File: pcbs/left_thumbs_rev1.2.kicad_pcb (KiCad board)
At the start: 2 copper layers, 93.5 x 38.7 mm, 12 parts

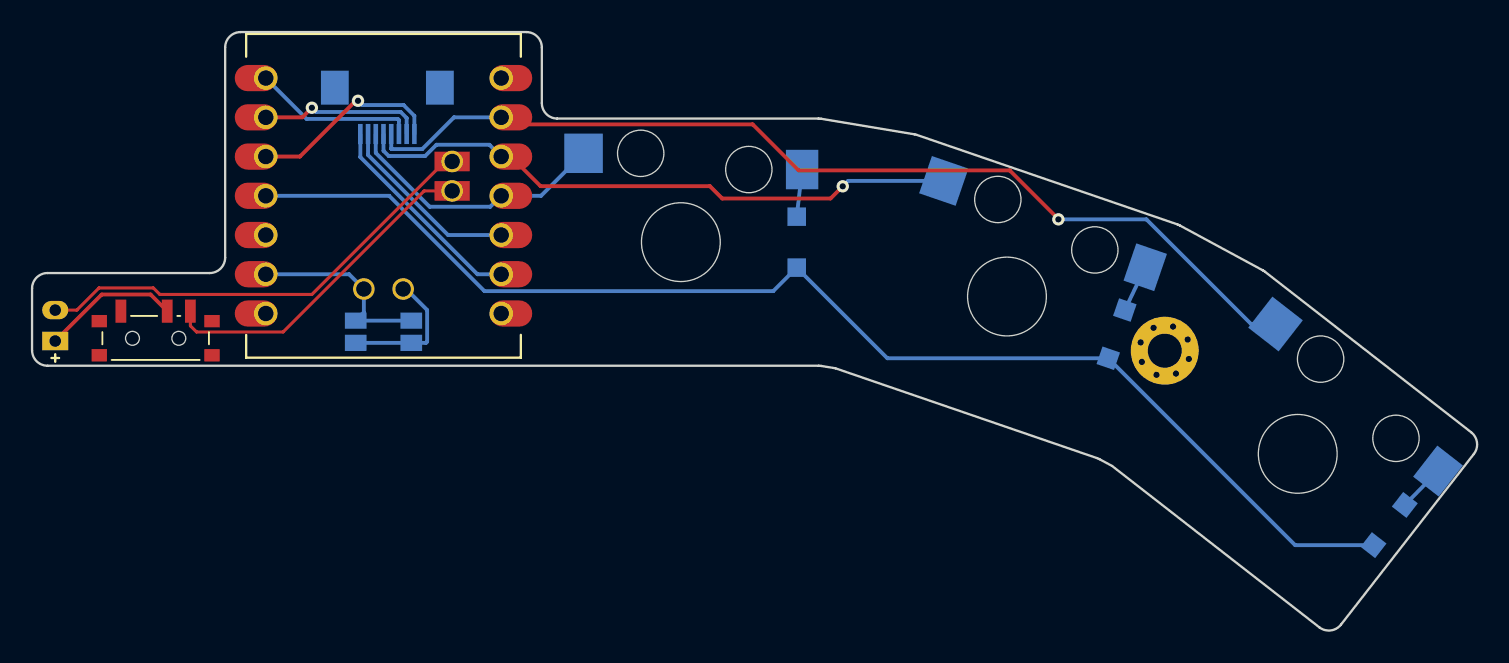
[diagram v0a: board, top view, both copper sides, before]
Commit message: Revision 1.2 - Socket was moved from middle home to inner home - Vertical column connections became thinner
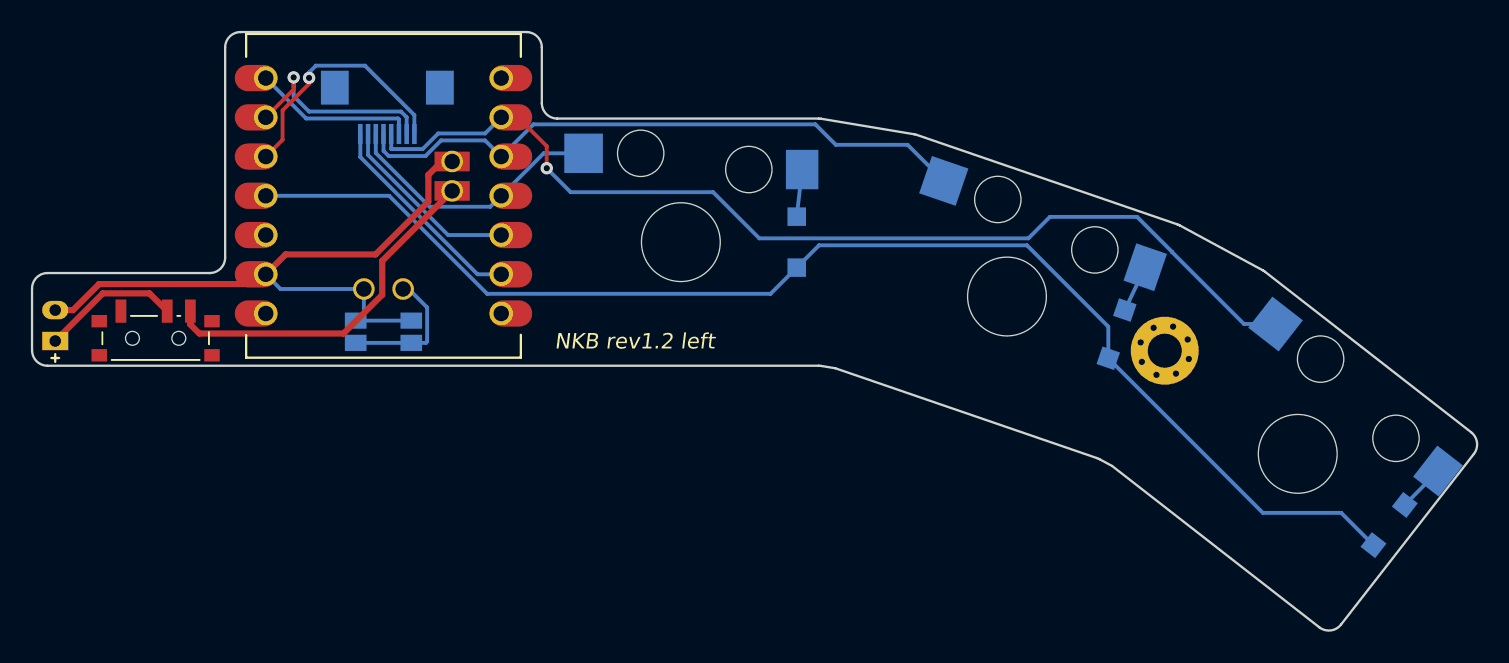
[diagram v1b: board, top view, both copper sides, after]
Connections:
- BAT1 pad 2: BATN -> GND
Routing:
- net GND: track 12.6 -> 43.8 mm
- net BATN: track 30.0 -> 0.00 mm
- net RLT3: track 12.7 -> 16.2 mm
- net RLT2: track 10.7 -> 13.5 mm
- net RLT4: track 82.3 -> 84.9 mm
- net CT5: track 64.6 -> 66.6 mm
- net BATP: track 21.8 -> 23.2 mm
- net CT4: track 39.7 -> 40.7 mm, vias 1 -> 0
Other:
- board text added: "NKB rev1.2 left"
